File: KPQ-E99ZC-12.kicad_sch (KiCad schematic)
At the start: 23 parts, among them J1 USB, J2 Chassis, J3 SWD, J4 Edge Connector, J5 Alternate Connector, SW1 BOOT, U1 USBLC6-2SC6, U2 XC6206P332MR-G, U3 STM32[C07/G0B]1KBT6

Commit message: Change R1 to combined THT/SMT footprint
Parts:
- R1: footprint Resistor_THT:R_Axial_DIN0207_L6.3mm_D2.5mm_P7.62mm_Horizontal -> BGK_Kicad:R_Combined_Axial_DIN0207_0603_1608Metric
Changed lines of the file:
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@@
 			)
 		)
-		(property "Footprint" "Resistor_THT:R_Axial_DIN0207_L6.3mm_D2.5mm_P7.62mm_Horizontal"
+		(property "Footprint" "BGK_Kicad:R_Combined_Axial_DIN0207_0603_1608Metric"
 			(at 240.792 88.9 90)
 			(effects

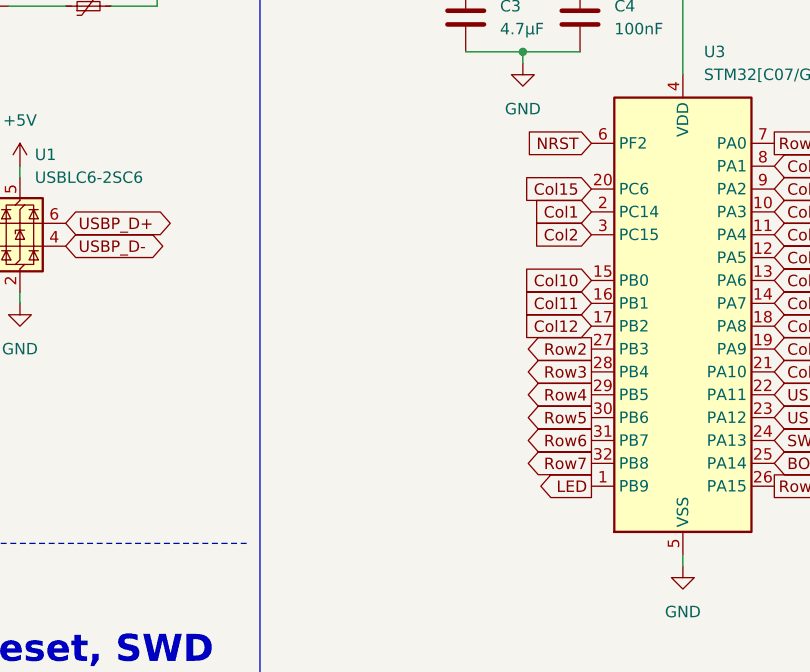
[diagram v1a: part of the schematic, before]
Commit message: Add pin notes to schematic
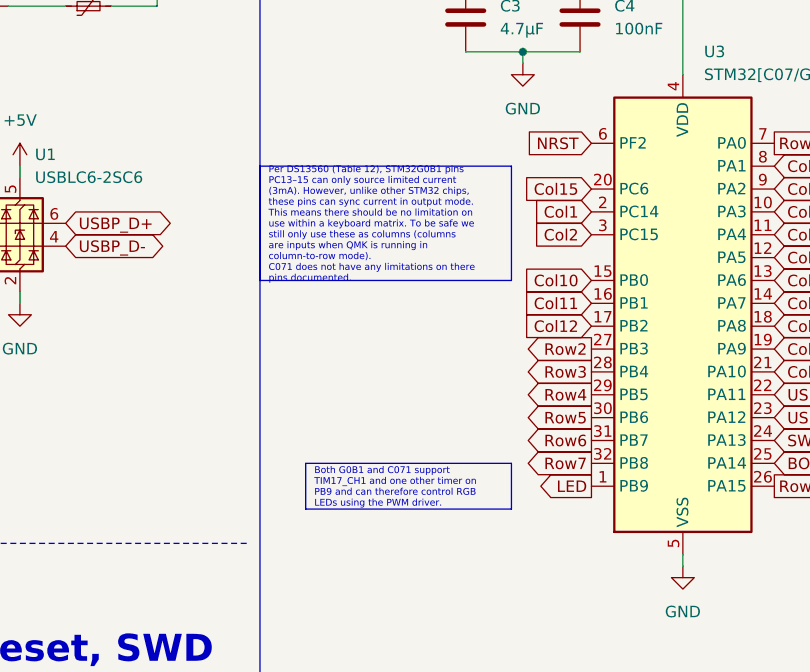
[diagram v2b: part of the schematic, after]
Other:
- company: (none) -> bgkendall
- title: (none) -> KPQ-E99ZC-12 Replacement PCB
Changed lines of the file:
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@@
 	(generator_version "9.0")
 	(paper "A4")
+	(title_block
+		(title "KPQ-E99ZC-12 Replacement PCB")
+		(date "2025-10-20")
+		(rev "1.0")
+		(company "bgkendall")
+	)
 	(text "Boot, Reset, SWD"
 		(exclude_from_sim no)
@@
 		)
 	)
+	(text_box "Both G0B1 and C071 support TIM17_CH1 and one other timer on PB9 and can therefore control RGB LEDs using the PWM driver."
+		(exclude_from_sim no)
+		(at 139.7 109.22 0)
+		(size 22.86 5.08)
+		(margins 0.9525 0.9525 0.9525 0.9525)
+		(stroke
+			(width 0)
+			(type solid)
+		)
+		(fill
+			(type none)
+		)
+		(effects
+			(font
+				(size 0.75 0.75)
+			)
+			(justify left)
+		)
+	)
+	(text_box "Per DS13560 (Table 12), STM32G0B1 pins PC13–15 can only source limited current (3mA). However, unlike other STM32 chips, these pins can sync current in output mode. This means there should be no limitation on use within a keyboard matrix. To be safe we still only use these as columns (columns are inputs when QMK is running in column-to-row mode).\nC071 does not have any limitations on there pins documented."
+		(exclude_from_sim no)
+		(at 134.62 76.2 0)
+		(size 27.94 12.7)
+		(margins 0.9525 0.9525 0.9525 0.9525)
+		(stroke
+			(width 0)
+			(type solid)
+		)
+		(fill
+			(type none)
+		)
+		(effects
+			(font
+				(size 0.75 0.75)
+			)
+			(justify left)
+		)
+	)

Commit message: Tidied schematic
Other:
- note added: "Boot & Reset"
- note added: "External Connections"
- note removed: "Boot, Reset, SWD"
- note removed: "Controller"
- note removed: "USB Cable Connection"
- moved on the sheet: C1, C2, C3, C4, C5, C6, C7, C8, F1, J1, J2, J3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

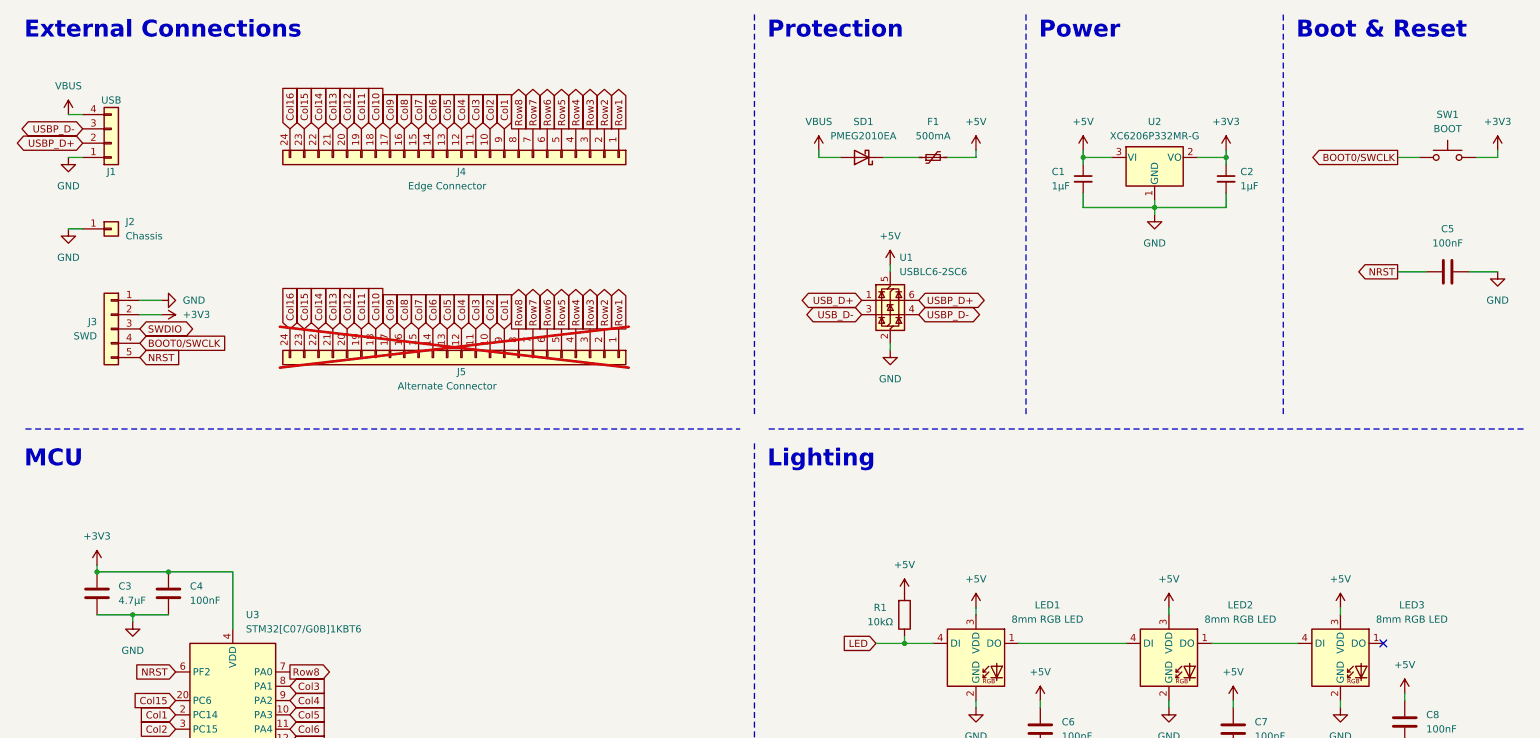
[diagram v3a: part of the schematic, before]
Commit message: Add boot resistor, tweak routing
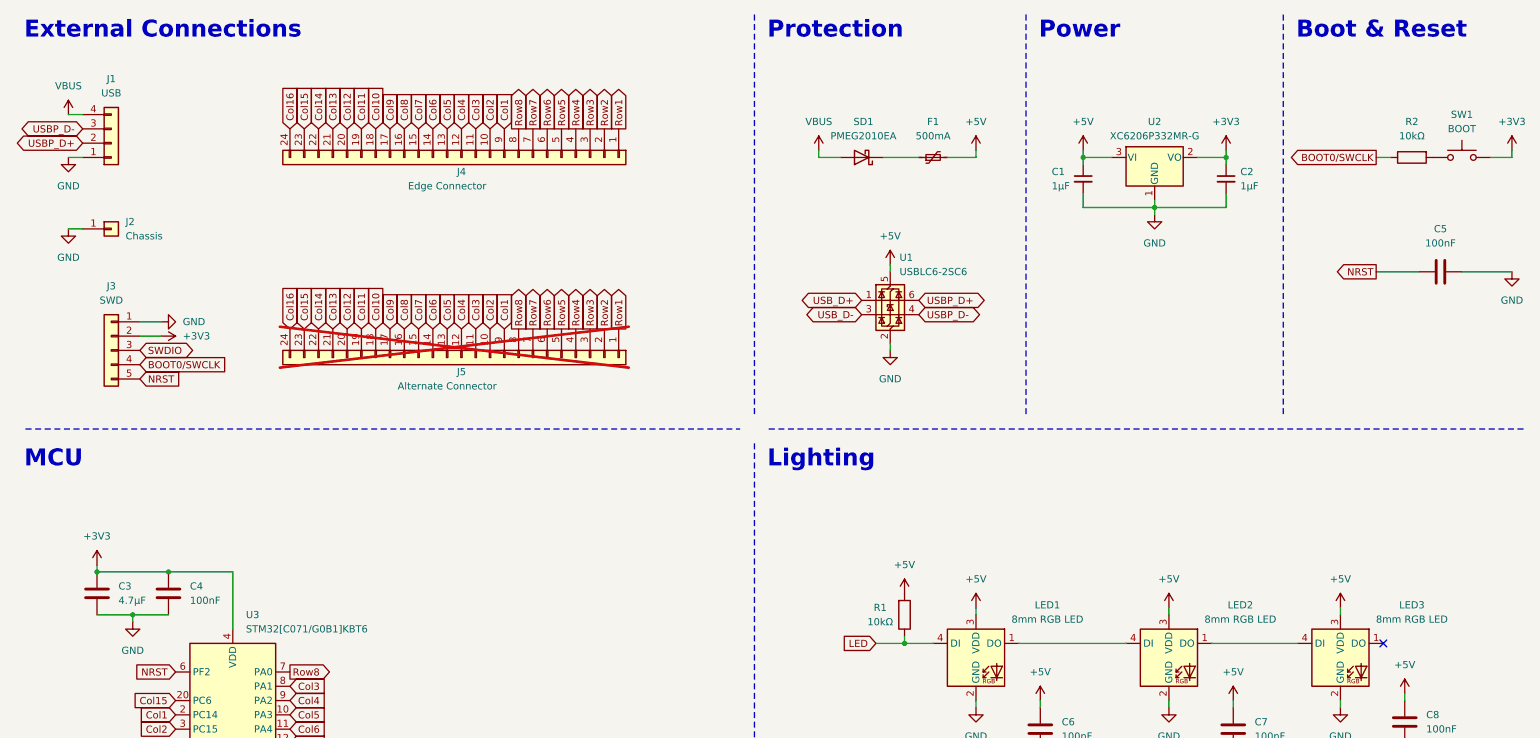
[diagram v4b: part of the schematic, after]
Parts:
- added R2: 10kΩ, BGK_Kicad:R_Combined_Axial_DIN0207_0603_1608Metric, symbol Device:R
- U3: value STM32[C07/G0B]1KBT6 -> STM32[C071/G0B1]KBT6
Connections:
- net BOOT0/SWCLK: now also R2.1; no longer SW1.1
- new net: R2.2, SW1.1
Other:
- moved on the sheet: C5, J3, SW1

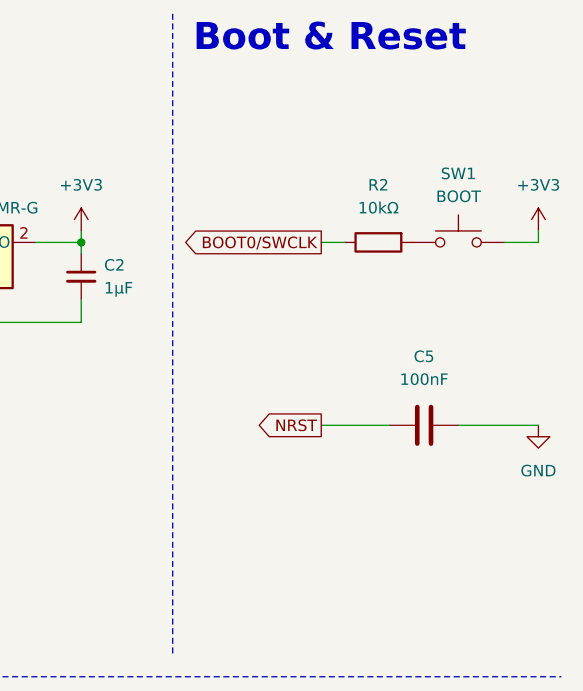
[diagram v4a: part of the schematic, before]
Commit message: Update boot circuit, tweak positioning and routing
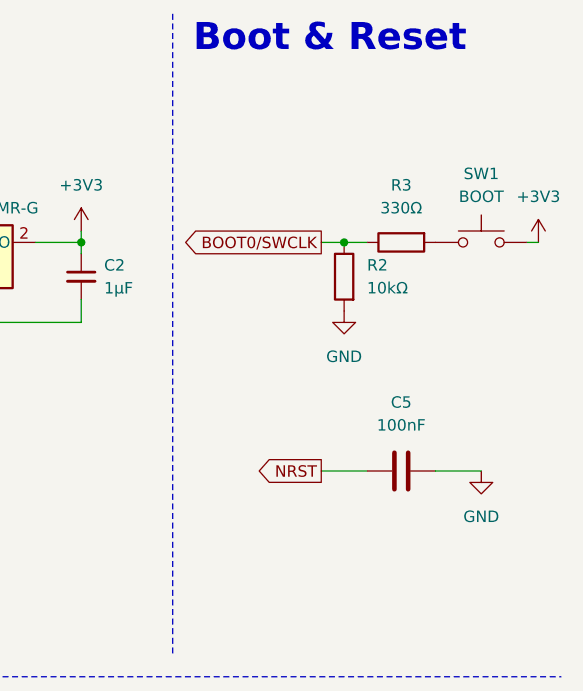
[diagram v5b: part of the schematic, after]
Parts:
- added R3: 330Ω, BGK_Kicad:R_Combined_Axial_DIN0207_0603_1608Metric, symbol Device:R
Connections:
- net BOOT0/SWCLK: now also R3.1
- net GND: now also R2.2
- net at SW1.1: now also R3.2; no longer R2.2
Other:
- moved on the sheet: C5, R2, SW1
